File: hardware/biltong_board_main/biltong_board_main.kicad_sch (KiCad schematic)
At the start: 46 parts, among them J1 Altech_AK300-3_P5.00mm, J11 JST_PH_B4B-PH-K_1x04_P2.00mm_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, J12 Conn_02x07_Odd_Even, J2 PinHeader_1x05_P2.54mm_Vertic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, J3 Altech_AK300-2_P5.00mm, J4 Altech_AK300-2_P5.00mm, J5 JST_PH_B4B-PH-K_1x04_P2.00mm_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, J6 JST_PH_B11B-PH-K_1x11_P2.00mm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, J7 JST_PH_B4B-PH-K_1x04_P2.00mm_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, J8 JST_PH_B4B-PH-K_1x04_P2.00mm_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

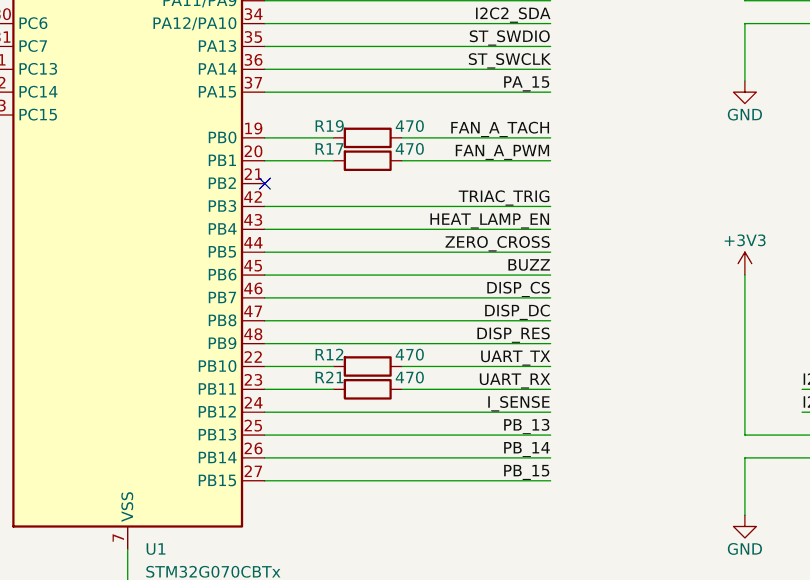
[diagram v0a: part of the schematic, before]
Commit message: swapped ADC pin
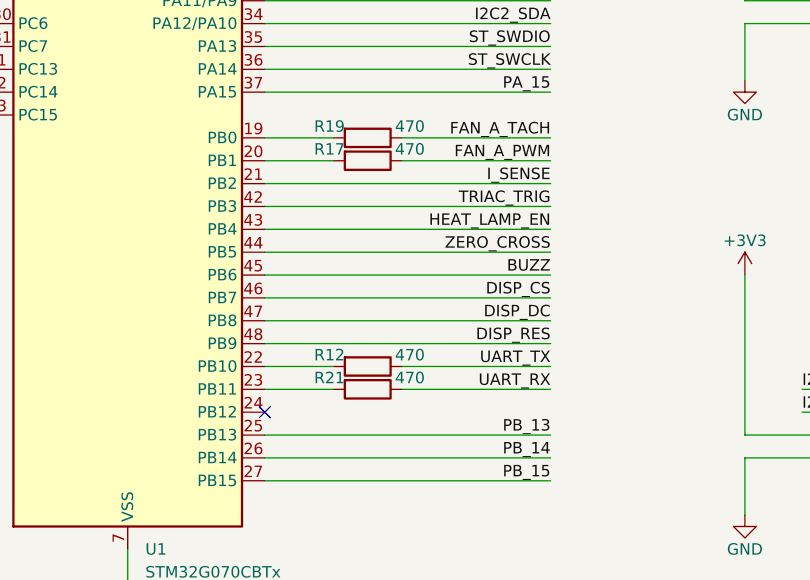
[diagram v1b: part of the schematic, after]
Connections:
- net I_SENSE: now also U1.21 (PB2); no longer U1.24 (PB12)

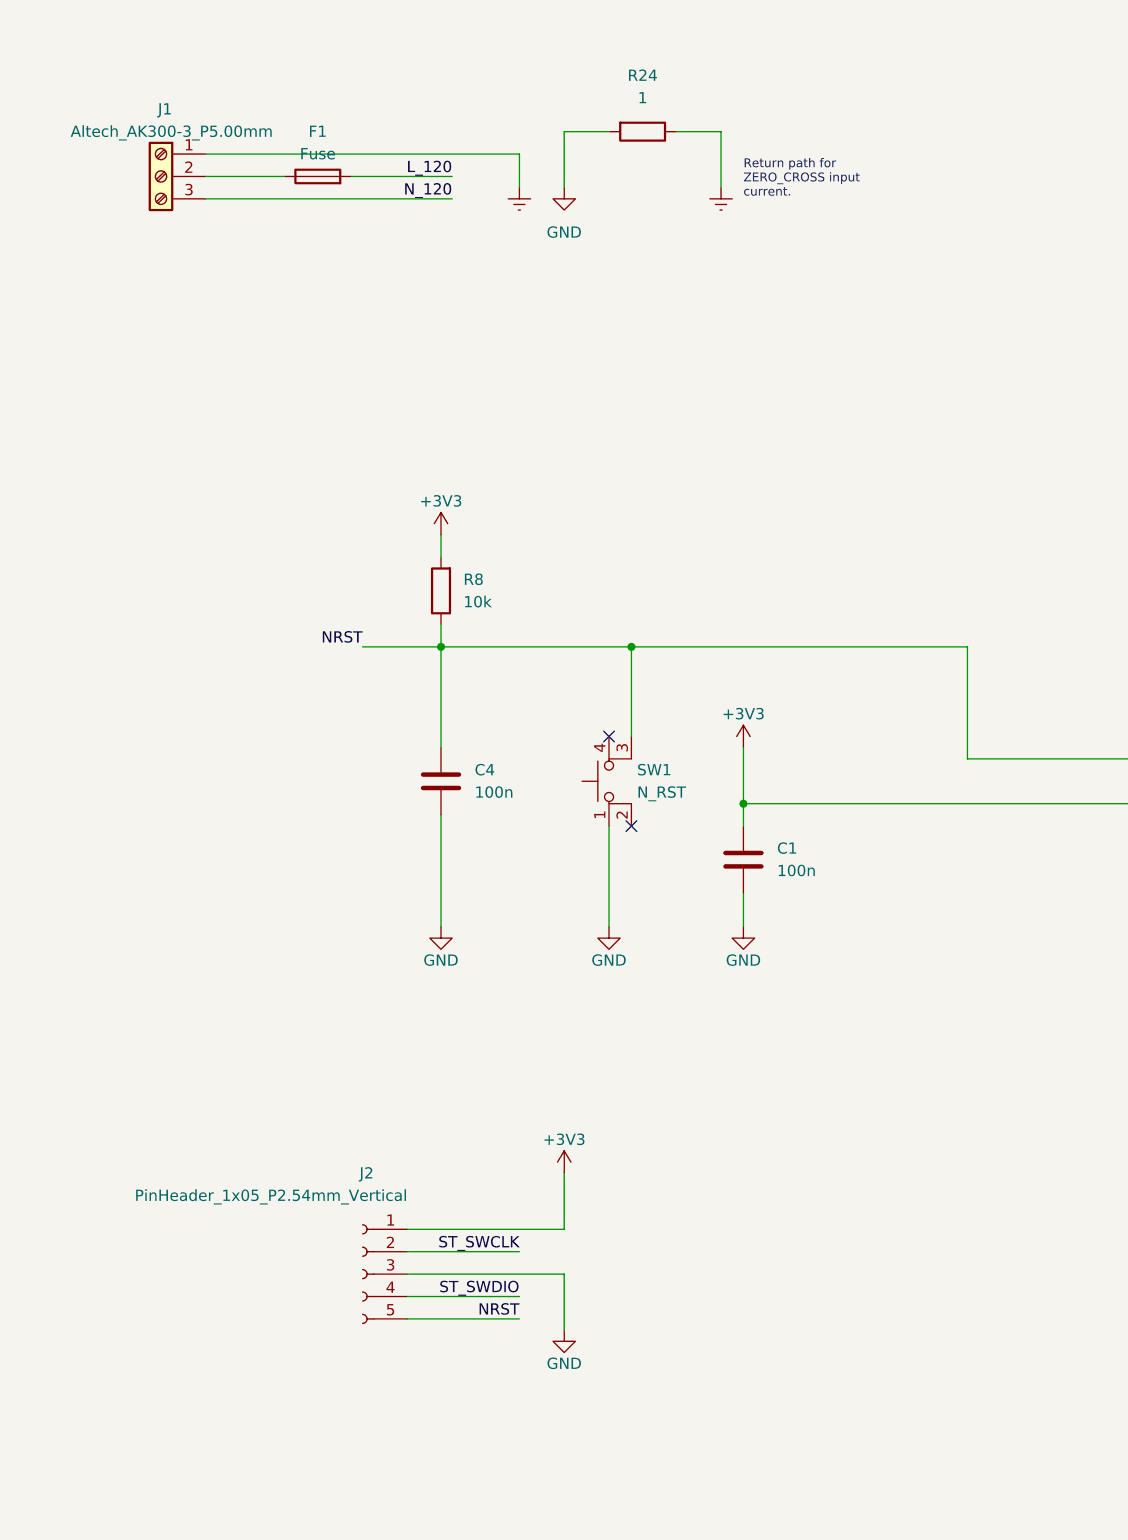
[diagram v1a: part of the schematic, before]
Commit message: generated BOM, swapped 10u cap size, README.md changes
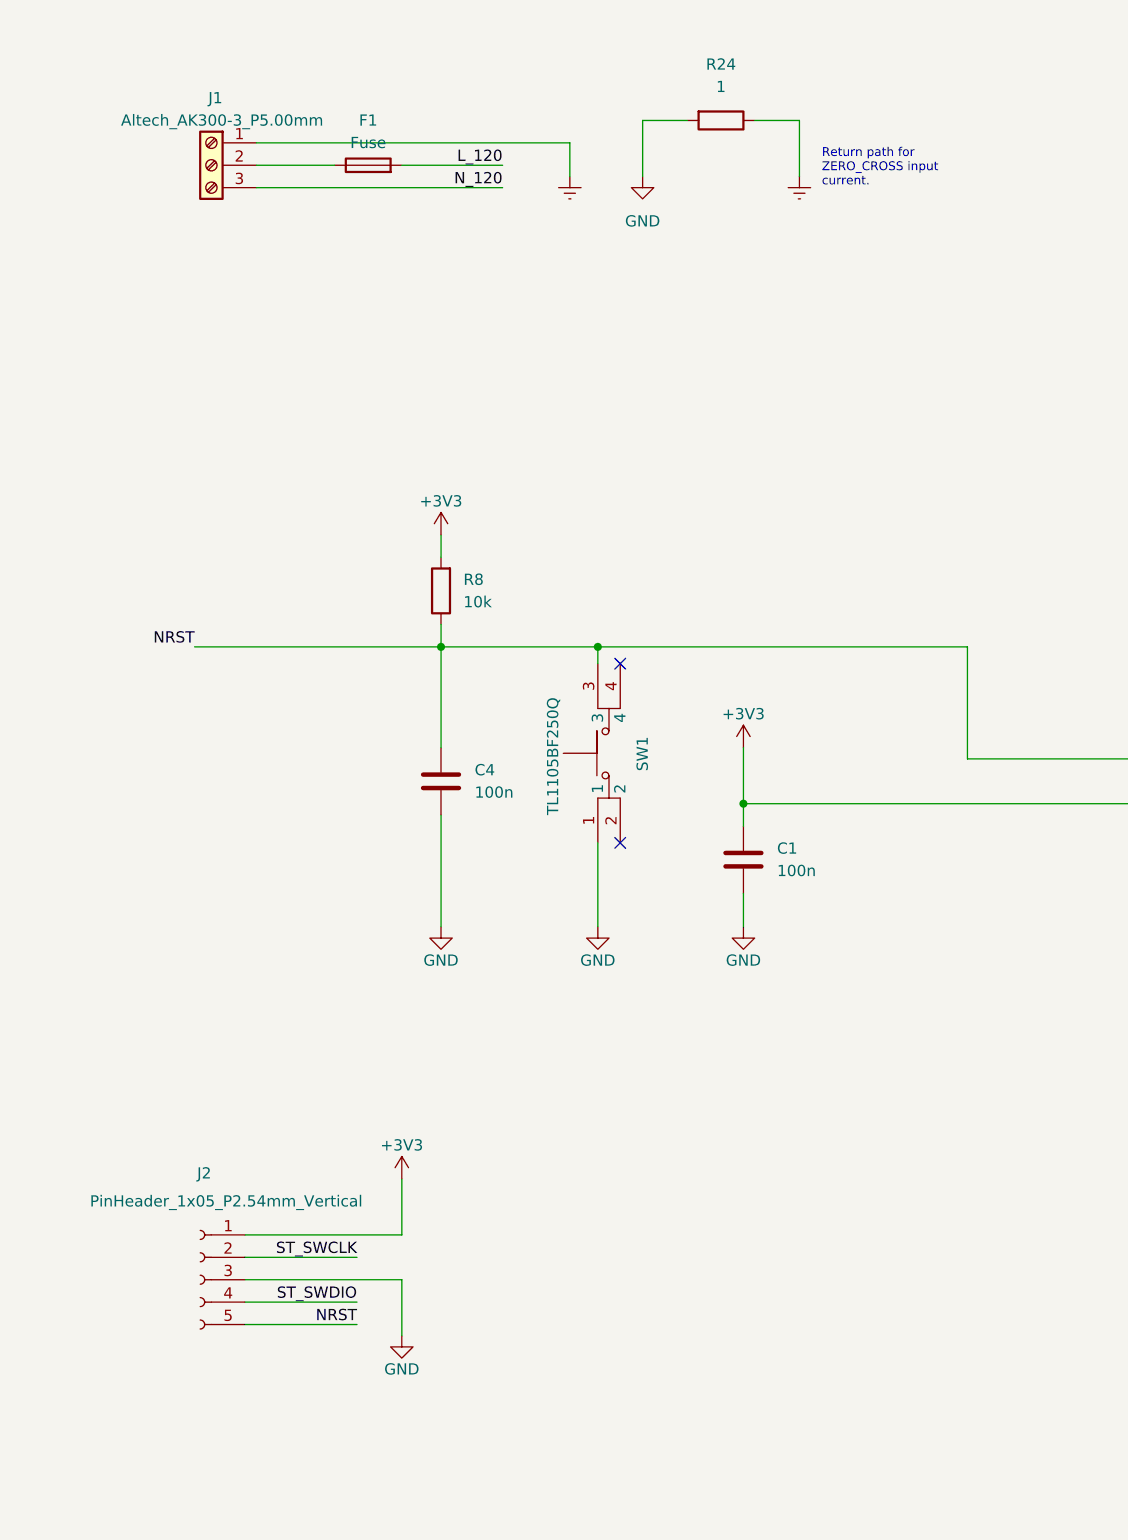
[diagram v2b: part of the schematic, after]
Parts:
- removed SW1: N_RST, BiltongBoardLib:SW_PUSH_6mm_H5mm_4_pin, symbol Switch:SW_MEC_5E
- added SW1: TL1105BF250Q, BiltongBoardLib:TL1105BF250Q, symbol BiltongBoard:TL1105BF250Q
- C15, C16: footprint Capacitor_THT:CP_Radial_D4.0mm_P2.00mm -> Capacitor_THT:CP_Radial_D5.0mm_P2.00mm
- H1, H2, H3, H4, H6, H7: now left out of the parts list
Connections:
- net GND: now also SW1.1
- net NRST: now also SW1.3
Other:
- moved on the sheet: F1, J1, J2, R24

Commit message: Fixed HS1 ground issue, missing schematic values, README.md update
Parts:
- added BT1: BH-98-1, BiltongBoardLib:BH-98-1, symbol Device:Battery_Cell
- F1: value Fuse -> 696106003002
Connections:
- net GND: now also BT1.2 (-)
- net VBAT: now also BT1.1 (+)
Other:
- note added: "F1: 5A 250VAC/125VAC"
- moved on the sheet: C1, C17, C18, C20, C4, C5, C6, C7, F1, H1, H2, H3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

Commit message: swapped zero cross pin for EXTI_2 line, HS1 recalculation
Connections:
- net ZERO_CROSS: now also U1.40 (PD2); no longer U1.44 (PB5)
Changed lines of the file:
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@@
   (junction (at 142.875 249.555) (diameter 0) (color 0 0 0 0)
   )
-  (no_connect (at 185.42 138.43))
+  (no_connect (at 215.9 171.45))
   (no_connect (at 185.42 151.13))
   (no_connect (at 76.2 125.095))
@@
     (stroke (width 0) (type default))
   )
-  (wire (pts (xy 247.65 171.45) (xy 215.9 171.45))
-    (stroke (width 0) (type default))
-  )
   (wire (pts (xy 363.22 130.81) (xy 386.08 130.81))
     (stroke (width 0) (type default))
@@
   )
   (wire (pts (xy 351.79 176.53) (xy 351.79 168.91))
+    (stroke (width 0) (type default))
+  )
+  (wire (pts (xy 153.67 138.43) (xy 185.42 138.43))
     (stroke (width 0) (type default))
   )
@@
     (effects (font (size 1.27 1.27)) (justify right bottom))
   )
+  (label "ZERO_CROSS" (at 153.67 138.43 0) (fields_autoplaced)
+    (effects (font (size 1.27 1.27)) (justify left bottom))
+  )
   (label "DISP_SCL" (at 276.86 83.82 0) (fields_autoplaced)
     (effects (font (size 1.27 1.27)) (justify left bottom))
@@
     (effects (font (size 1.27 1.27)) (justify right bottom))
   )
-  (label "ZERO_CROSS" (at 247.65 171.45 180) (fields_autoplaced)
-    (effects (font (size 1.27 1.27)) (justify right bottom))
-  )

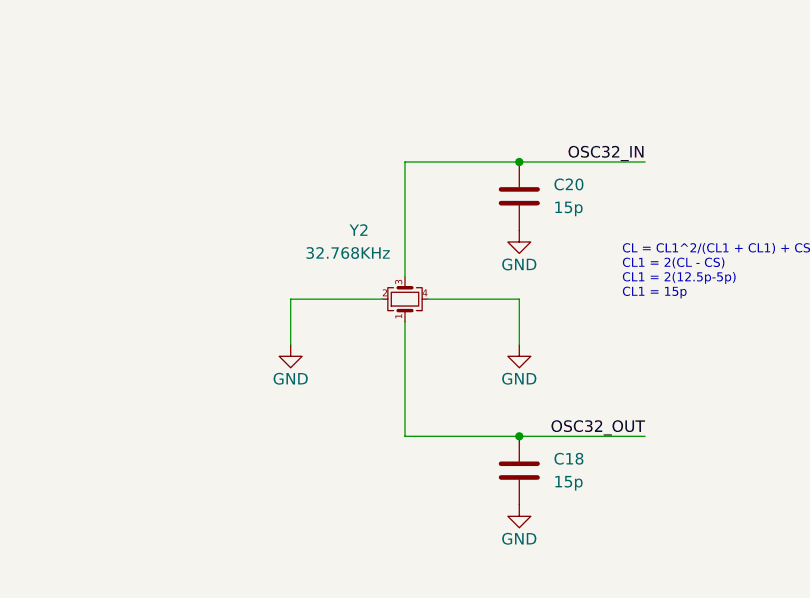
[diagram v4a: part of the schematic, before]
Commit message: RTC oscillator fix, lamp connector new model & footprints
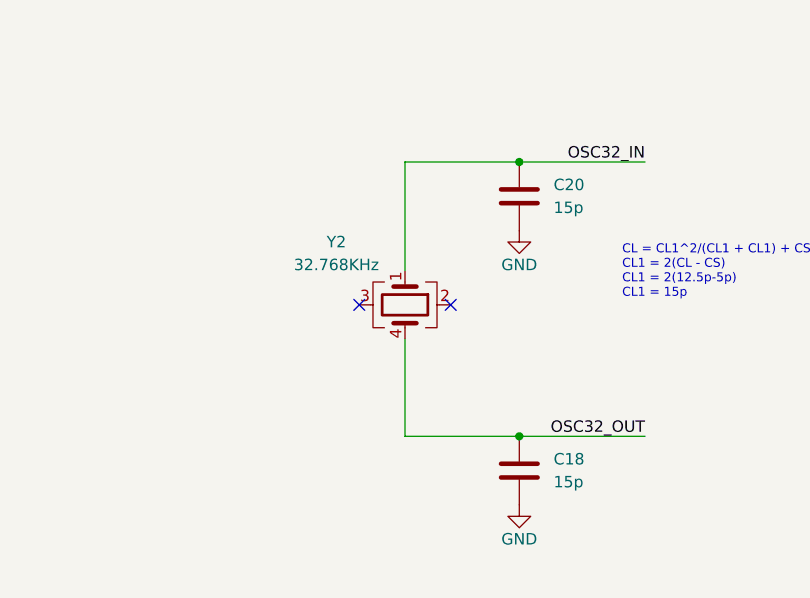
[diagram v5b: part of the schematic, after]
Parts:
- removed Y2: 32.768KHz, BiltongBoardLib:Crystal_SMD_Abracon_ABS25-4Pin_8.0x3.8mm_w_model, symbol Device:Crystal_GND24_Small
- added Y2: 32.768KHz, BiltongBoardLib:Crystal_SMD_Abracon_ABS25-4Pin_8.0x3.8mm_w_model, symbol Device:Crystal_GND23
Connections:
- net OSC32_IN: now also Y2.1
- net OSC32_OUT: now also Y2.4
- no-connect marks 7 -> 9
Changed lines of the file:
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@@
   )
   (no_connect (at 215.9 171.45))
+  (no_connect (at 125.095 234.95))
   (no_connect (at 185.42 151.13))
   (no_connect (at 76.2 125.095))
+  (no_connect (at 135.255 234.95))
   (no_connect (at 185.42 140.97))
   (no_connect (at 215.9 115.57))
@@
     (stroke (width 0) (type default))
   )
+  (wire (pts (xy 130.175 238.76) (xy 130.175 249.555))
+    (stroke (width 0) (type default))
+  )
   (wire (pts (xy 347.98 225.425) (xy 323.85 225.425))
     (stroke (width 0) (type default))
@@
     (stroke (width 0) (type default))
   )
-  (wire (pts (xy 117.475 234.315) (xy 117.475 239.395))
-    (stroke (width 0) (type default))
-  )
   (wire (pts (xy 358.14 116.84) (xy 358.14 119.38))
     (stroke (width 0) (type default))
@@
     (stroke (width 0) (type default))
   )
-  (wire (pts (xy 130.175 219.075) (xy 130.175 231.775))
+  (wire (pts (xy 130.175 219.075) (xy 130.175 231.14))
     (stroke (width 0) (type default))
   )
@@
     (stroke (width 0) (type default))
   )
-  (wire (pts (xy 142.875 234.315) (xy 132.715 234.315))
-    (stroke (width 0) (type default))
-  )
   (wire (pts (xy 288.29 115.57) (xy 288.29 116.84))
     (stroke (width 0) (type default))
   )
-  (wire (pts (xy 127.635 234.315) (xy 117.475 234.315))
-    (stroke (width 0) (type default))
-  )
   (wire (pts (xy 294.64 124.46) (xy 294.64 129.54))
     (stroke (width 0) (type default))
@@
     (stroke (width 0) (type default))
   )
-  (wire (pts (xy 130.175 236.855) (xy 130.175 249.555))
-    (stroke (width 0) (type default))
-  )
   (wire (pts (xy 215.9 140.97) (xy 247.65 140.97))
     (stroke (width 0) (type default))
@@
   )
   (wire (pts (xy 153.67 148.59) (xy 185.42 148.59))
-    (stroke (width 0) (type default))
-  )
-  (wire (pts (xy 142.875 234.315) (xy 142.875 239.395))
     (stroke (width 0) (type default))
   )
@@
     )
   )
-  (symbol (lib_id "power:GND") (at 142.875 239.395 0) (unit 1)
-    (in_bom yes) (on_board yes) (dnp no)
-    (property "Reference" "#PWR051" (at 142.875 245.745 0)
-      (effects (font (size 1.27 1.27)) hide)
-    )
-    (property "Value" "GND" (at 142.875 243.205 0)
-      (effects (font (size 1.27 1.27)))
-    )
-    (property "Footprint" "" (at 142.875 239.395 0)
-      (effects (font (size 1.27 1.27)) hide)
-    )
-    (property "Datasheet" "" (at 142.875 239.395 0)
-      (effects (font (size 1.27 1.27)) hide)
-    )
-    (pin "1")
-    (instances
-      (project "biltong_board_main"
-        (path "/0a1e579b-8207-4868-883c-1f24490f13ce"
-          (reference "#PWR051") (unit 1)
-        )
-      )
-    )
-  )
   (symbol (lib_id "Connector:Screw_Terminal_01x02") (at 391.16 45.72 0) (unit 1)
     (in_bom yes) (on_board yes) (dnp no)
@@
         (path "/0a1e579b-8207-4868-883c-1f24490f13ce"
           (reference "J3") (unit 1)
+        )
+      )
+    )
+  )
+  (symbol (lib_id "Device:Crystal_GND23") (at 130.175 234.95 270) (unit 1)
+    (in_bom yes) (on_board yes) (dnp no)
+    (property "Reference" "Y2" (at 122.555 227.965 90)
+      (effects (font (size 1.27 1.27)))
+    )
+    (property "Value" "32.768KHz" (at 122.555 230.505 90)
+      (effects (font (size 1.27 1.27)))
+    )
+    (property "Footprint" "BiltongBoardLib:Crystal_SMD_Abracon_ABS25-4Pin_8.0x3.8mm_w_model" (at 130.175 234.95 0)
+      (effects (font (size 1.27 1.27)) hide)
+    )
+    (property "Datasheet" "https://www.digikey.ca/en/products/detail/abracon-llc/ABS25-32-768KHZ-T/675361" (at 130.175 234.95 0)
+      (effects (font (size 1.27 1.27)) hide)
+    )
+    (pin "1")
+    (pin "2")
+    (pin "3")
+    (pin "4")
+    (instances
+      (project "biltong_board_main"
+        (path "/0a1e579b-8207-4868-883c-1f24490f13ce"
+          (reference "Y2") (unit 1)
         )
       )
@@
     )
   )
-  (symbol (lib_id "power:GND") (at 117.475 239.395 0) (unit 1)
-    (in_bom yes) (on_board yes) (dnp no)
-    (property "Reference" "#PWR050" (at 117.475 245.745 0)
-      (effects (font (size 1.27 1.27)) hide)
-    )
-    (property "Value" "GND" (at 117.475 243.205 0)
-      (effects (font (size 1.27 1.27)))
-    )
-    (property "Footprint" "" (at 117.475 239.395 0)
-      (effects (font (size 1.27 1.27)) hide)
-    )
-    (property "Datasheet" "" (at 117.475 239.395 0)
-      (effects (font (size 1.27 1.27)) hide)
-    )
-    (pin "1")
-    (instances
-      (project "biltong_board_main"
-        (path "/0a1e579b-8207-4868-883c-1f24490f13ce"
-          (reference "#PWR050") (unit 1)
-        )
-      )
-    )
-  )
   (symbol (lib_id "Device:R") (at 227.33 133.35 270) (unit 1)
     (in_bom yes) (on_board yes) (dnp no)
@@
         )
       )
-    )
-  )
-  (symbol (lib_id "Device:Crystal_GND24_Small") (at 130.175 234.315 270) (mirror x) (unit 1)
-    (in_bom yes) (on_board yes) (dnp no)
-    (property "Reference" "Y2" (at 125.095 226.695 90)
-      (effects (font (size 1.27 1.27)))
-    )
-    (property "Value" "32.768KHz" (at 123.825 229.235 90)
-      (effects (font (size 1.27 1.27)))
-    )
-    (property "Footprint" "BiltongBoardLib:Crystal_SMD_Abracon_ABS25-4Pin_8.0x3.8mm_w_model" (at 130.175 234.315 0)
-      (effects (font (size 1.27 1.27)) hide)
-    )
-    (property "Datasheet" "https://www.digikey.ca/en/products/detail/abracon-llc/ABS25-32-768KHZ-T/675361" (at 130.175 234.315 0)
-      (effects (font (size 1.27 1.27)) hide)
-    )
-    (pin "1")
-    (pin "2")
-    (pin "3")
-    (pin "4")
-    (instances
-      (project "biltong_board_main"
-        (path "/0a1e579b-8207-4868-883c-1f24490f13ce"
-          (reference "Y2") (unit 1)
-        )
-      )
-      (project "Tracker_Charger_V1"
-        (path "/38c4babf-9cde-4e06-a603-1df616028c2e"
-          (reference "Y1") (unit 1)
-        )
-      )
